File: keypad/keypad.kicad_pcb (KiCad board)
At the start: 2 copper layers, 59 parts, among them J1 AVR-ISP-6, SW1 num, SW10 #5, SW11 #6, SW12 plu1, SW13 #1, SW14 #2, SW15 #3, SW16 ent0, SW17 #0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

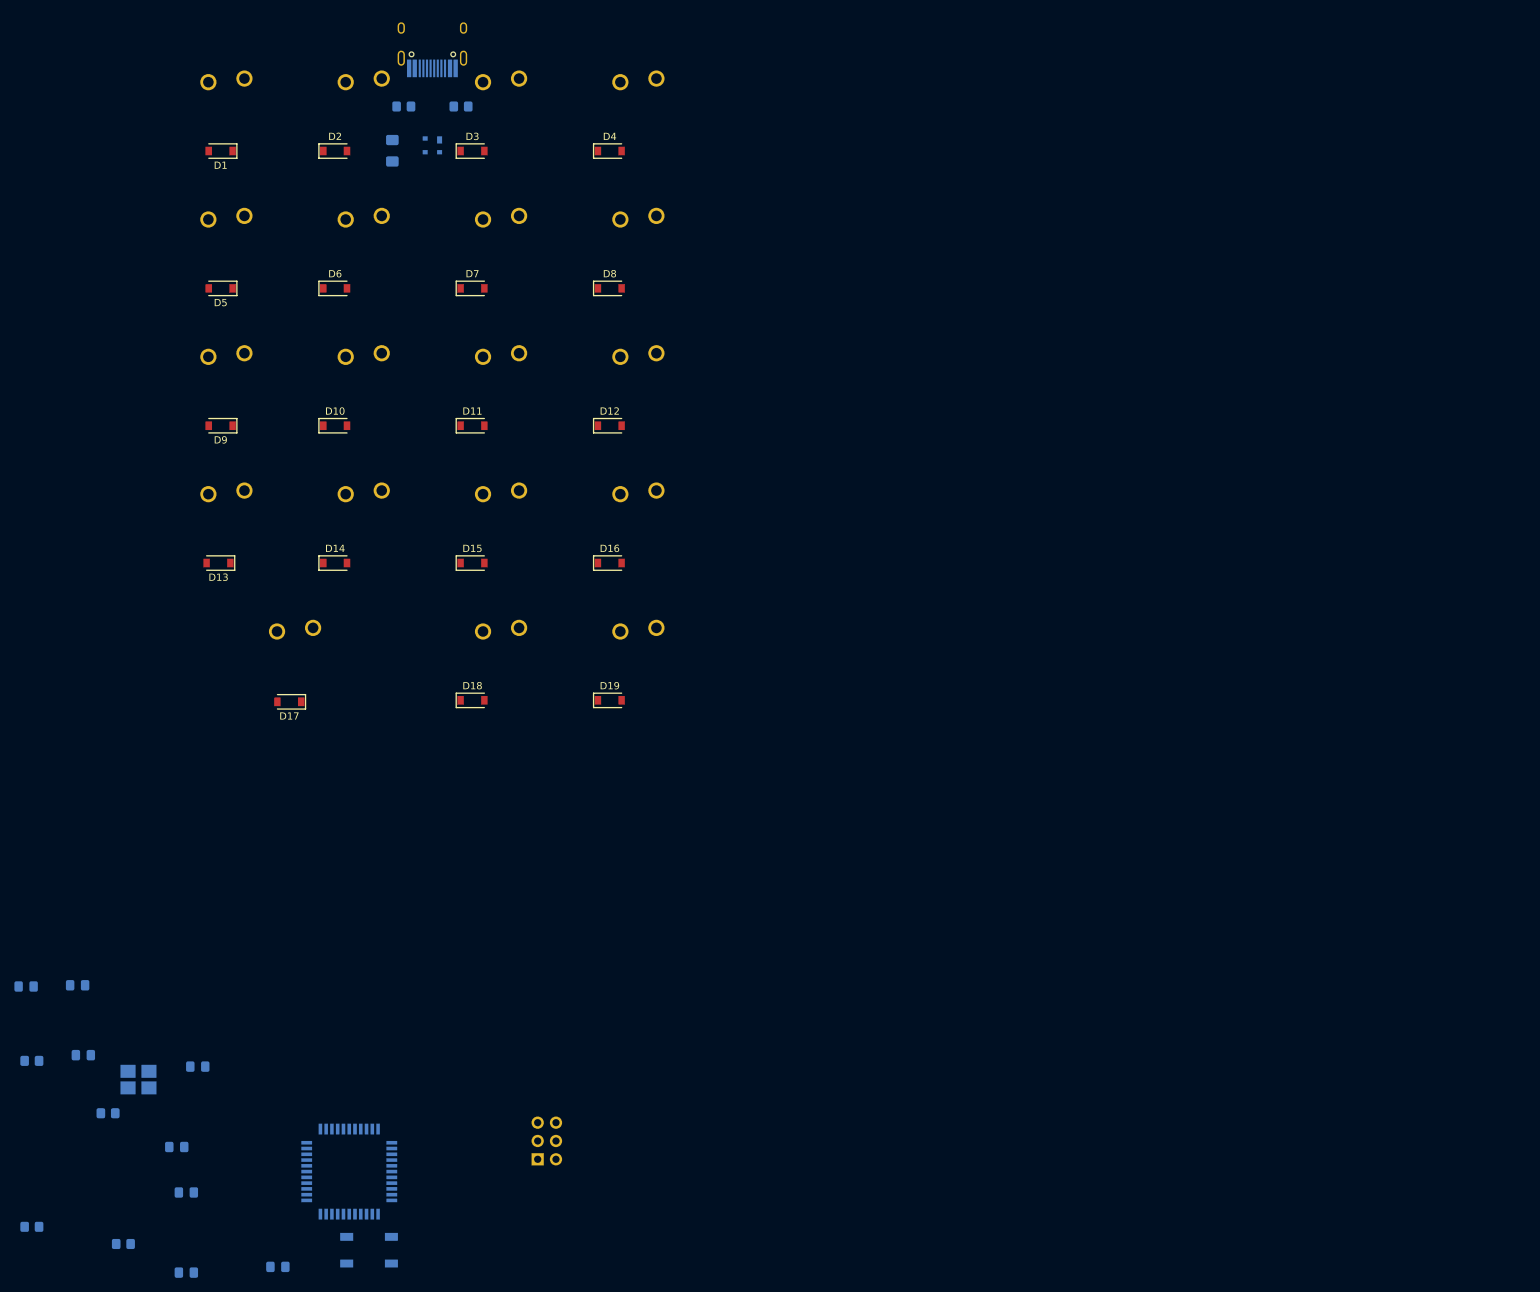
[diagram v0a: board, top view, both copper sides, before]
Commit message: Add Main layout
Note that some of the layering is probably wrong. Check that again.
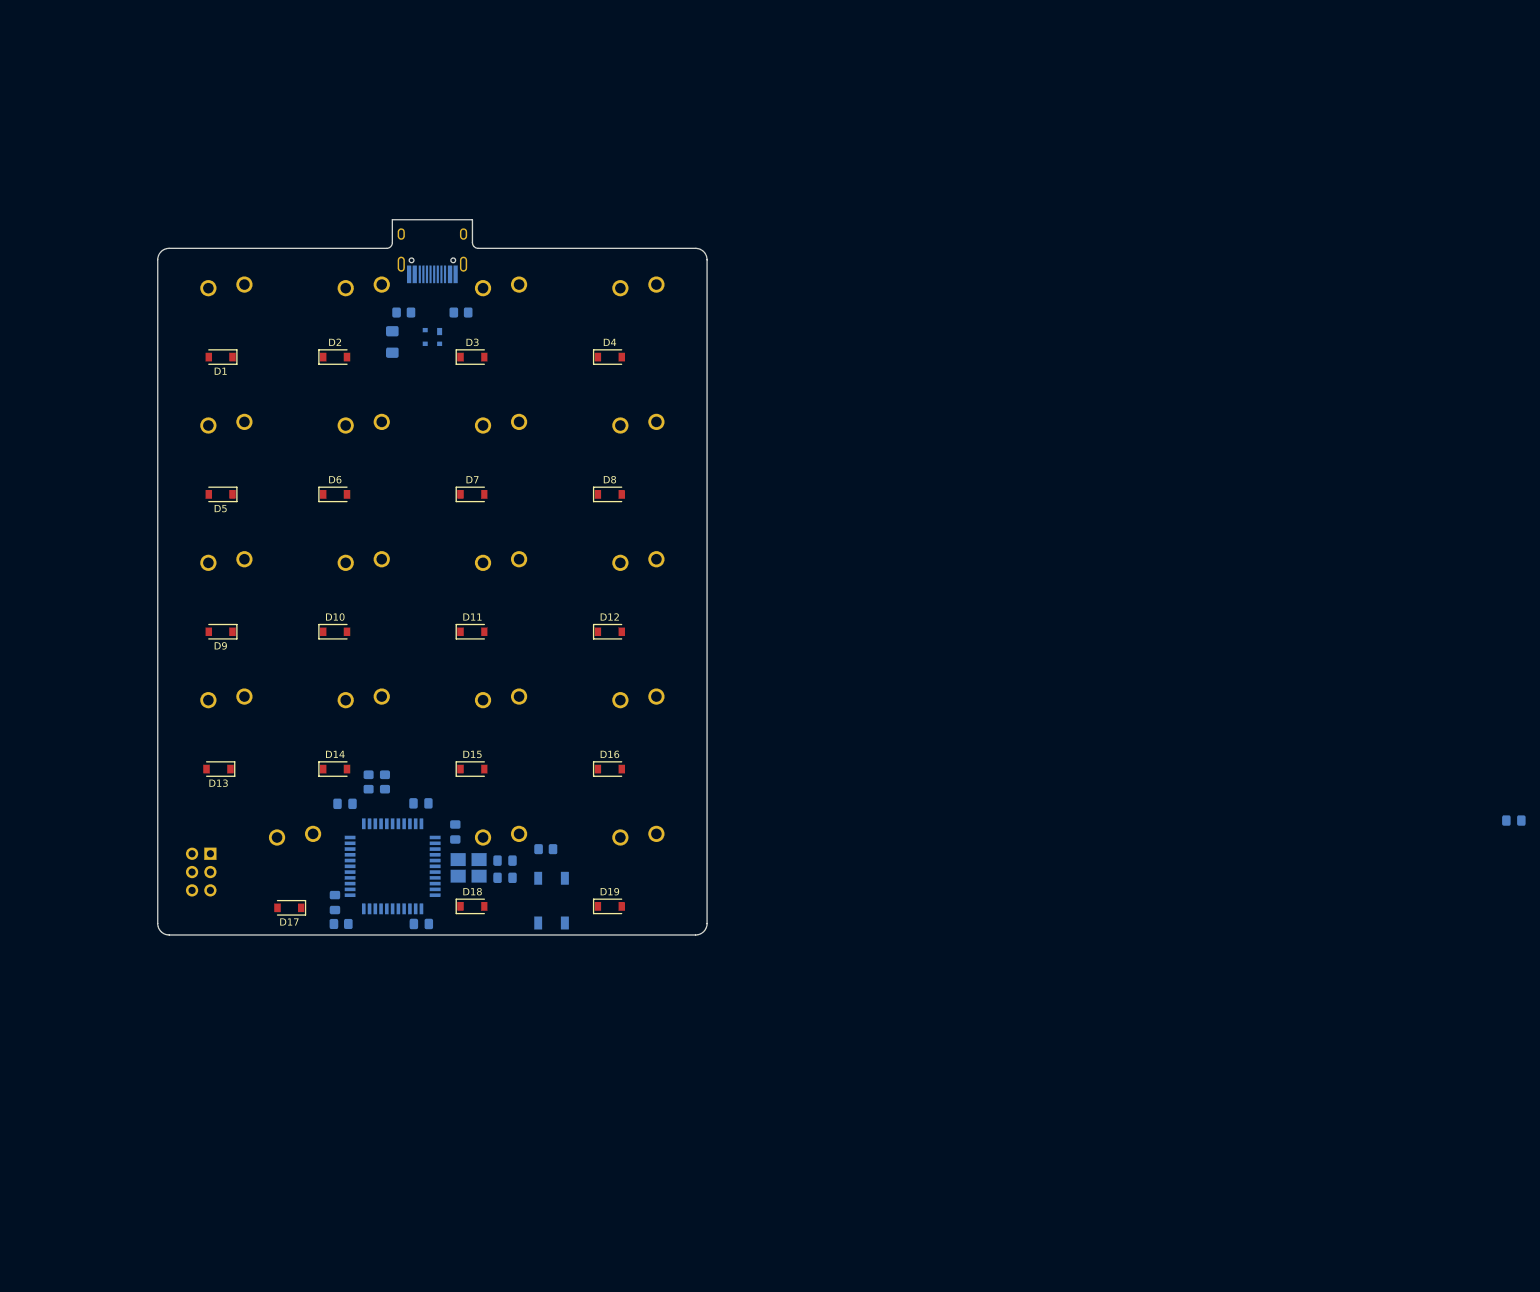
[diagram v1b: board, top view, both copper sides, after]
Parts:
- moved C3 201.1 mm to (223.8, 133.3)
- moved R2 77.4 mm to (65.0, 128.0), turned to -90 degrees
- moved R1 77.1 mm to (89.5, 137.3)
- moved R3 73.6 mm to (67.2, 128.0), turned to -90 degrees
- moved C8 72.8 mm to (72.2, 131.0)
- moved C2 64.6 mm to (83.9, 138.9), turned to 0 degrees
- moved C1 62.1 mm to (83.9, 141.3), turned to 0 degrees
- moved J1 60.7 mm to (41.8, 140.5), turned to 0 degrees
- moved C6 58.3 mm to (77.0, 134.9), turned to -90 degrees
- moved SW20 54.7 mm to (90.3, 144.5), turned to -90 degrees
- moved Y1 54.4 mm to (78.8, 139.9)
- moved C7 44.8 mm to (61.7, 131.0)
- moved C5 44.4 mm to (60.3, 144.7), turned to 90 degrees
- moved U2 42.8 mm to (68.3, 139.7), turned to -90 degrees
- moved R4 41.6 mm to (61.2, 147.7)
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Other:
- board outline added: 76.2 x 99.2 mm

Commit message: Fixed Layering
Also as a note, there was a rogue 1uF capacitor which I now just placed under the usb, out of the way. It may be needed later.
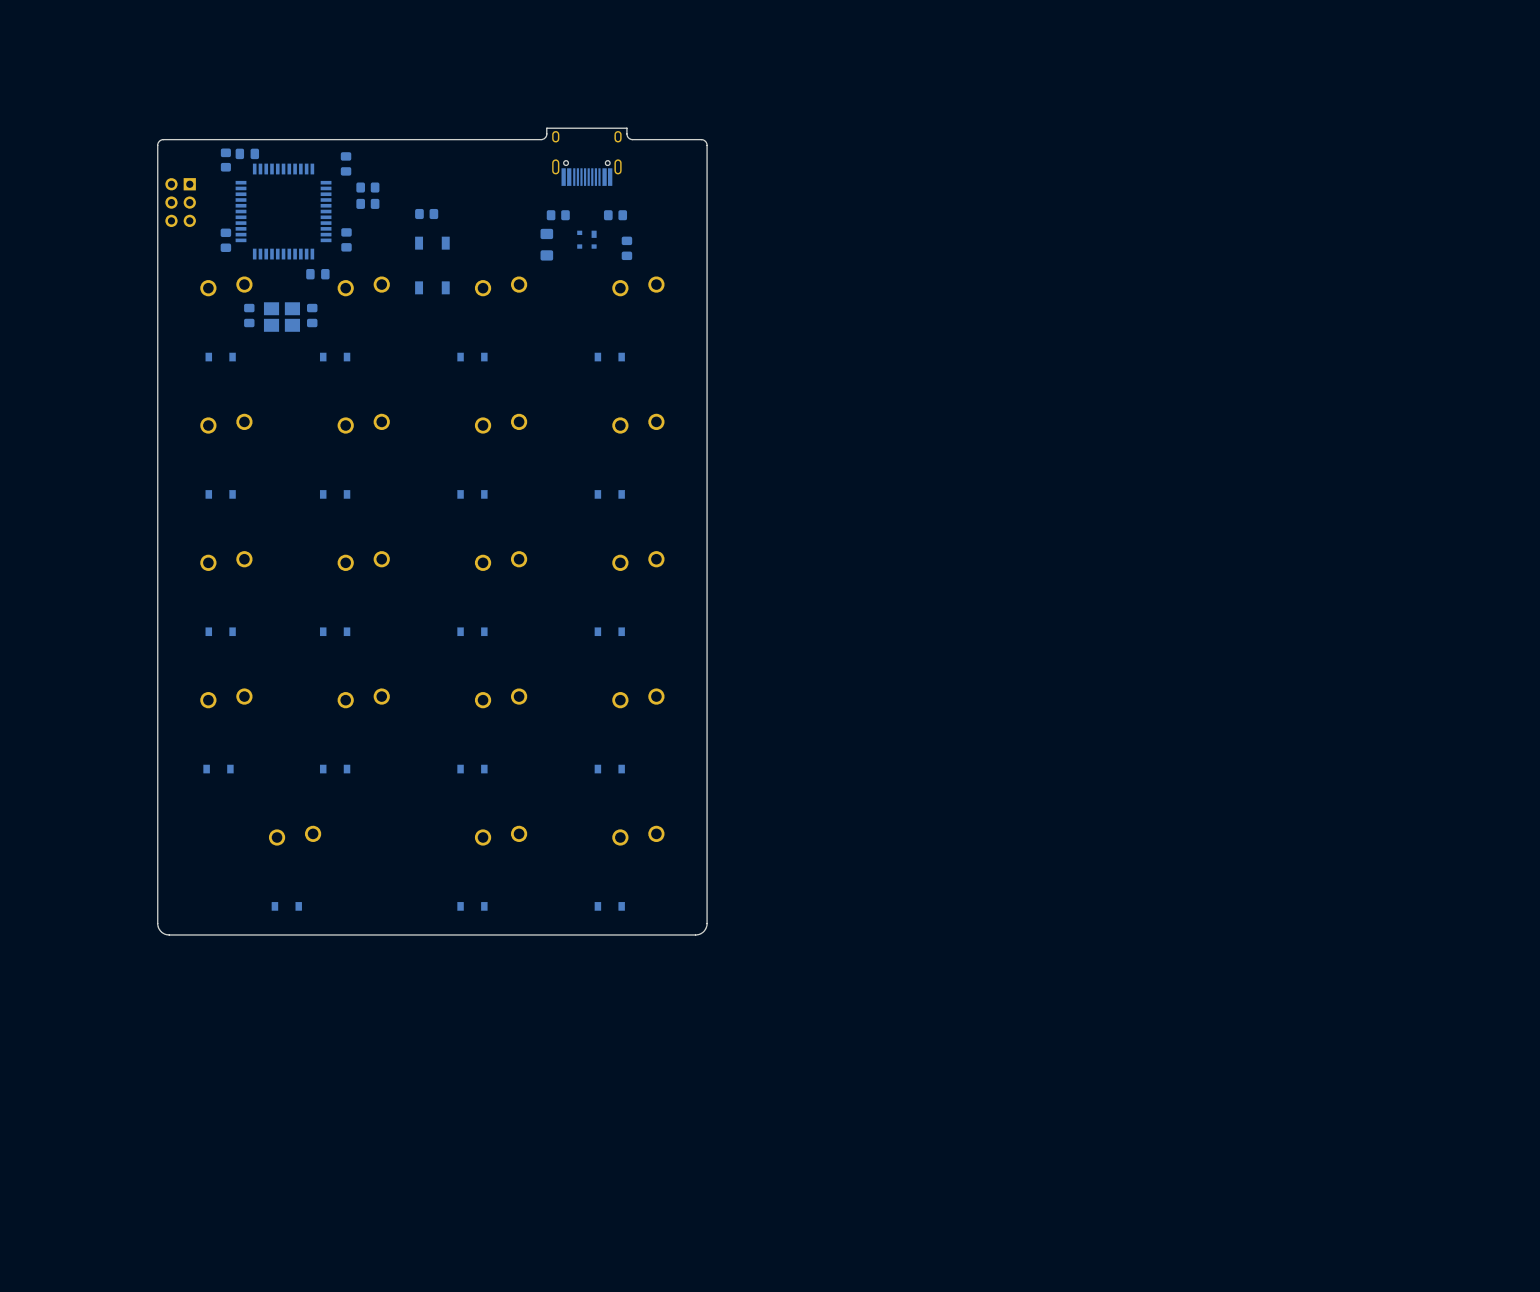
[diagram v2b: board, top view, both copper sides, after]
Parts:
- D1, D10, D11, D12, D13, D14, D15, D16, D17, D18, D19, D2, D3, D4, D5, D6, D7, D8, D9: moved to B.Cu
- moved C3 146.4 mm to (100.8, 54.0), turned to 90 degrees
- moved R4 107.2 mm to (45.2, 41.7), turned to 90 degrees
- moved C5 104.6 mm to (48.1, 40.9), turned to 0 degrees
- moved C4 98.6 mm to (45.2, 52.9), turned to -90 degrees
- moved J1 92.9 mm to (38.9, 47.6)
- moved U2 92.1 mm to (53.2, 48.9), turned to 180 degrees
- moved SW20 89.6 mm to (73.8, 56.4)
- moved R1 89.6 mm to (73.0, 49.2)
- moved C7 88.8 mm to (61.8, 42.3), turned to 90 degrees
- moved C1 85.7 mm to (48.4, 63.3), turned to -90 degrees
- moved R2 82.5 mm to (64.9, 45.5), turned to 180 degrees
- moved Y1 80.7 mm to (53.0, 63.5), turned to 0 degrees
- moved R3 80.2 mm to (64.9, 47.8), turned to 180 degrees
- moved C2 80.2 mm to (57.1, 63.3), turned to 90 degrees
- moved C6 79.7 mm to (57.9, 57.6), turned to 180 degrees
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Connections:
- U2 pad 18: unconnected-(U2-Pad18) -> row4
- U2 pad 19: unconnected-(U2-Pad19) -> row3
- U2 pad 20: unconnected-(U2-Pad20) -> row2
- U2 pad 21: unconnected-(U2-Pad21) -> row1
- U2 pad 22: unconnected-(U2-Pad22) -> row0
- U2 pad 37: row4 -> unconnected-(U2-Pad37)
- U2 pad 38: row3 -> unconnected-(U2-Pad38)
- U2 pad 39: row2 -> unconnected-(U2-Pad39)
- U2 pad 40: row1 -> unconnected-(U2-Pad40)
- U2 pad 41: row0 -> unconnected-(U2-Pad41)
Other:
- board size 76.2 x 99.2 mm -> 76.2 x 111.9 mm

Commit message: Started Routing
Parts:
- moved J1 35.2 mm to (69.8, 31.0)
- moved SW20 27.7 mm to (80.2, 29.4)
- moved R1 27.7 mm to (79.4, 22.2)
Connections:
- net Net-(R2-Pad1) renamed DN
- net Net-(R3-Pad1) renamed DP
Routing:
- net col0: track 0.00 -> 80.1 mm
- net col3: track 0.00 -> 76.2 mm
- net col2: track 0.00 -> 76.2 mm
- net col1: track 0.00 -> 57.2 mm
- net DP: track 0.00 -> 7.61 mm
- net DN: track 0.00 -> 5.89 mm

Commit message: Removed Routing and Replaced components
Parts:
- moved SW20 33.0 mm to (53.2, 48.4)
- moved J1 33.0 mm to (42.9, 50.0)
- moved R1 33.0 mm to (52.4, 41.3)
- moved USB1 23.2 mm to (115.7, 46.8), turned to -90 degrees
- moved C2 20.1 mm to (77.2, 63.3)
- moved C6 20.1 mm to (78.0, 57.6)
- moved C8 20.1 mm to (82.0, 52.8)
- moved C1 20.1 mm to (68.5, 63.3)
- moved C4 20.1 mm to (65.2, 52.9)
- moved C5 20.1 mm to (68.2, 40.9)
- moved C7 20.1 mm to (81.9, 42.3)
- moved R2 20.1 mm to (84.9, 45.5)
- moved R3 20.1 mm to (84.9, 47.8)
- moved R4 20.1 mm to (65.2, 41.7)
- moved U2 20.1 mm to (73.2, 48.9)
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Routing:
- net DP: track 7.61 -> 0.00 mm
- net DN: track 5.89 -> 0.00 mm

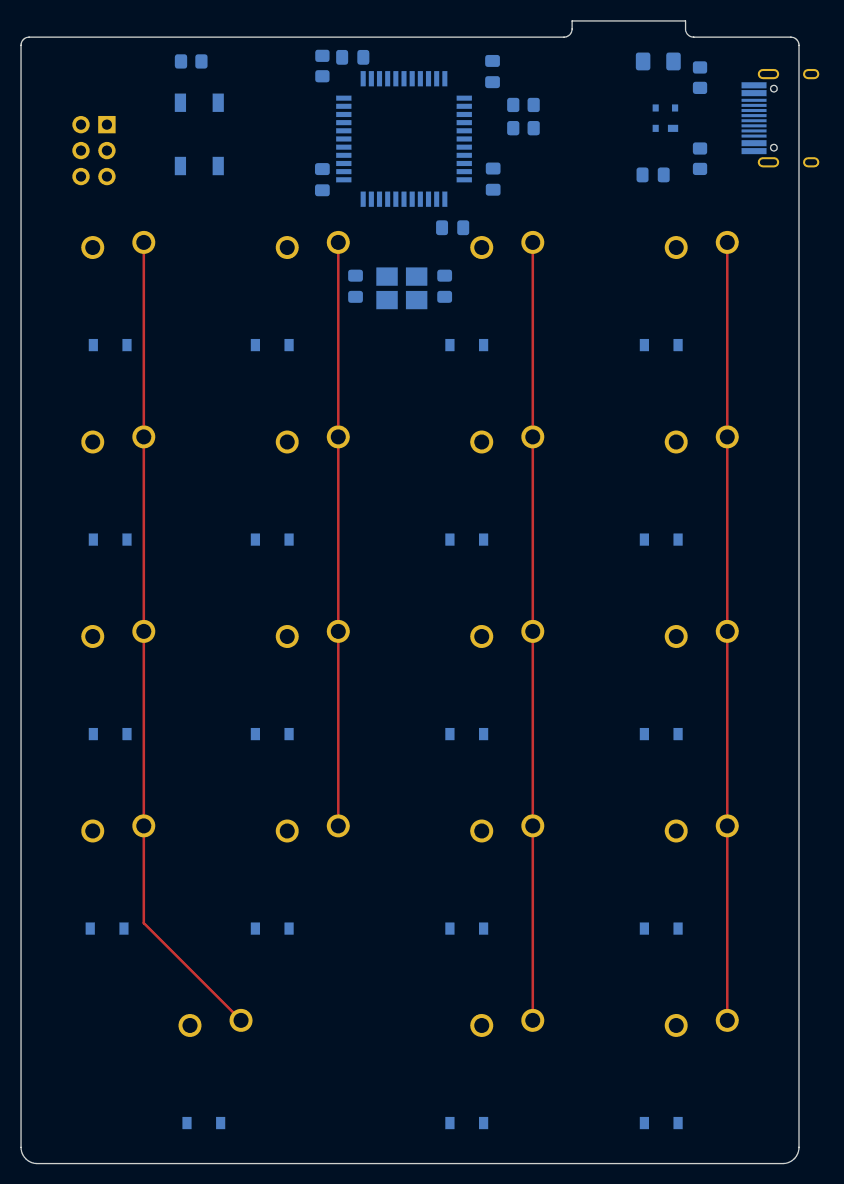
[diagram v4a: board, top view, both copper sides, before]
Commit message: Routed D-Pair and Matrix
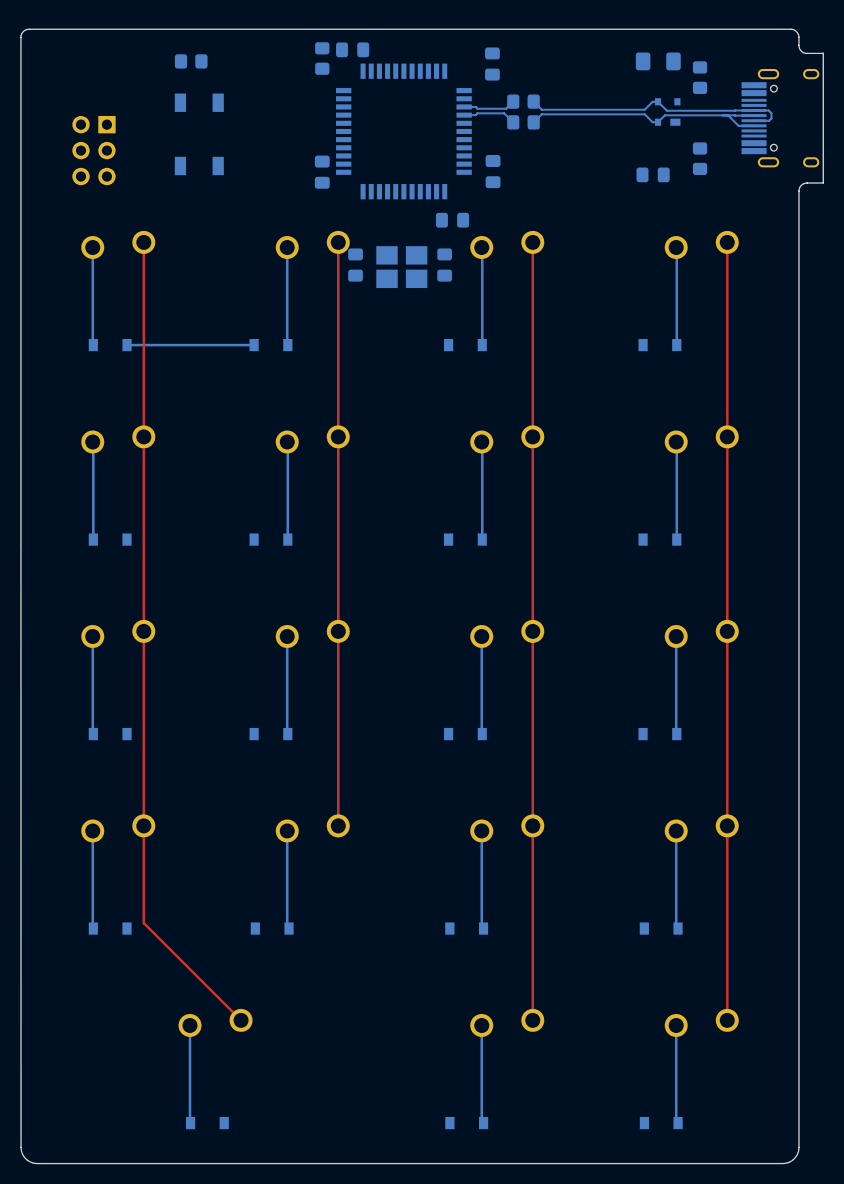
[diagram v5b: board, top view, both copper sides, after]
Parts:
- moved C1 2.08 mm to (68.5, 61.2)
- moved C2 2.08 mm to (77.2, 61.2)
- moved Y1 2.08 mm to (73.0, 61.4)
- moved C5 0.74 mm to (68.2, 40.1)
- moved C6 0.74 mm to (78.0, 56.8)
- moved C7 0.74 mm to (81.9, 41.5)
- moved R4 0.74 mm to (65.2, 41.0)
- moved C4 0.74 mm to (65.2, 52.1)
- moved C8 0.74 mm to (82.0, 52.1)
- moved U2 0.74 mm to (73.2, 48.1)
- moved U1 0.65 mm to (99.1, 46.2)
- moved R3 0.56 mm to (84.9, 47.2)
- moved D17 0.35 mm to (54.0, 145.3)
- moved R2 0.33 mm to (84.9, 45.2)
- moved D13 0.30 mm to (44.5, 126.2)
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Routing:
- net DN: track 0.00 -> 26.8 mm
- net DP: track 0.00 -> 26.1 mm
- net row0: track 0.00 -> 12.4 mm
- net Net-(D1-Pad2): track 0.00 -> 9.95 mm
- net Net-(D19-Pad2): track 0.00 -> 9.63 mm
- net Net-(D18-Pad2): track 0.00 -> 9.63 mm
- net Net-(D16-Pad2): track 0.00 -> 9.63 mm
- net Net-(D15-Pad2): track 0.00 -> 9.63 mm
- net Net-(D14-Pad2): track 0.00 -> 9.63 mm
- net Net-(D8-Pad2): track 0.00 -> 9.61 mm
- net Net-(D7-Pad2): track 0.00 -> 9.61 mm
- net Net-(D6-Pad2): track 0.00 -> 9.61 mm
- net Net-(D5-Pad2): track 0.00 -> 9.61 mm
- net Net-(D4-Pad2): track 0.00 -> 9.61 mm
- net Net-(D3-Pad2): track 0.00 -> 9.61 mm
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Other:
- board size 76.2 x 111.9 mm -> 78.6 x 111.1 mm
